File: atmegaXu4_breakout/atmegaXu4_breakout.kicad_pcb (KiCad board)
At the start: 2 copper layers, 20 x 50.5 mm, 36 parts, among them J1 USB_C_Receptacle_USB2.0, J2 Header-West, J3 Header-East, J4 AVR-ISP-6, SW1 nUSR_PB, SW2 nRST_PB, U1 ATmega32U4-MU, U2 AP2127K-3.3, Y1 ABM11-16.000MHZ-12-N1G-T

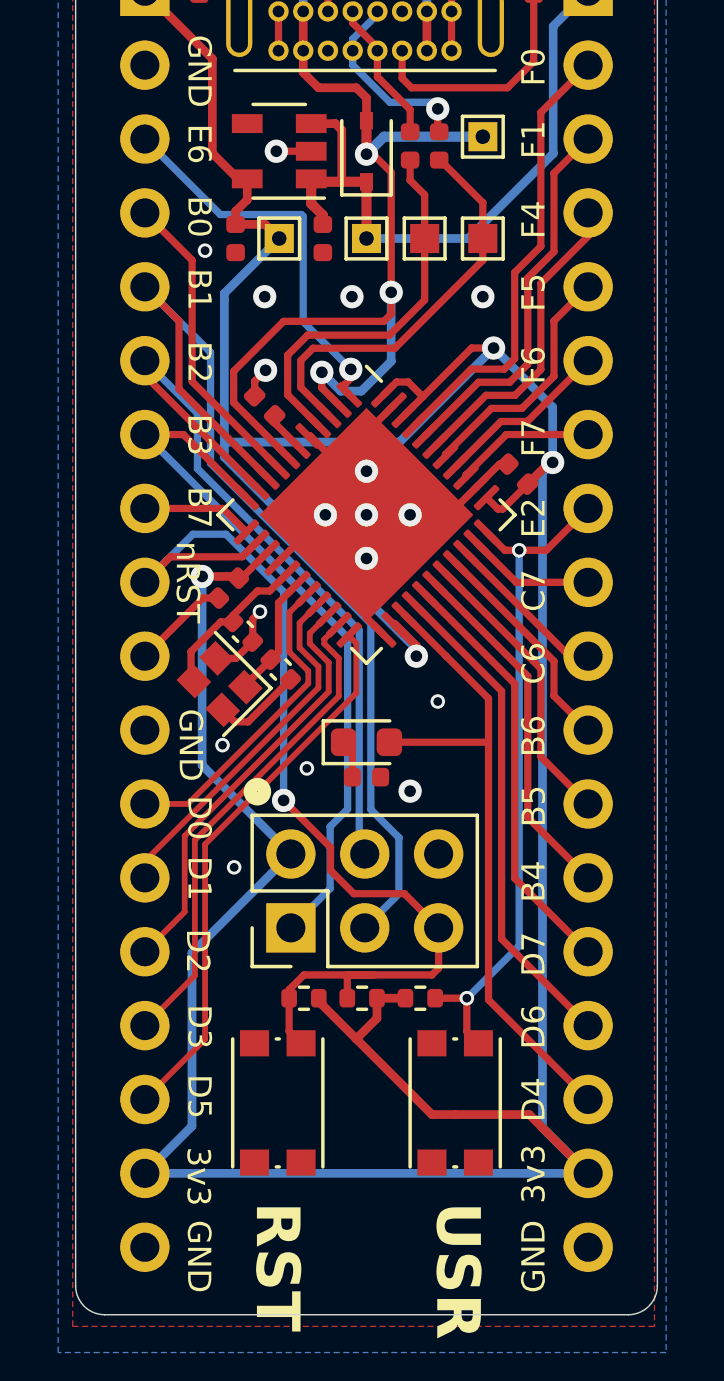
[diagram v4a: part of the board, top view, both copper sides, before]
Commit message: Added CI utils for automating releases
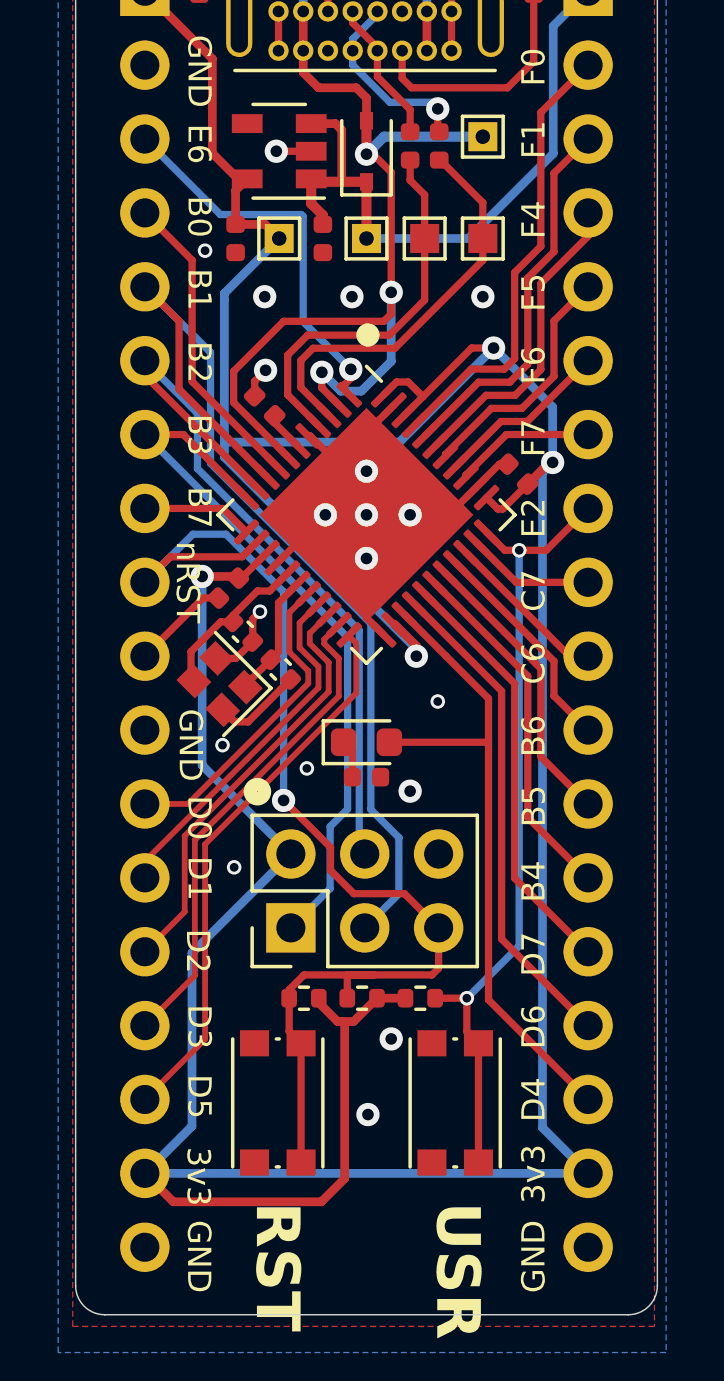
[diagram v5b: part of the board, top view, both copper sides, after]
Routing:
- net PE2: track 23.3 -> 27.4 mm
- net ~{RESET}: track 36.0 -> 40.1 mm
- net +3V3: track 139.2 -> 141.6 mm
- net GND: vias 19 -> 21
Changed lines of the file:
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@@
       (stroke (width 0) (type solid)) (fill solid) (layer "B.SilkS"))
   )
+  (gr_circle (center 146.8 85.6) (end 147 85.6)
+    (stroke (width 0.4) (type default)) (fill none) (layer "F.SilkS"))
   (gr_circle (center 143 101.3) (end 143.2 101.2)
     (stroke (width 0.5) (type solid)) (fill none) (layer "F.SilkS"))
@@
   (via (at 141.8 99.7) (size 0.5) (drill 0.3) (layers "F.Cu" "B.Cu") (free) (net 2))
   (via (at 149.2 98.2) (size 0.5) (drill 0.3) (layers "F.Cu" "B.Cu") (free) (net 2))
+  (via (at 147.6 109.8) (size 0.8) (drill 0.4) (layers "F.Cu" "B.Cu") (net 2))
   (via (at 139.250019 70.281845) (size 0.8) (drill 0.4) (layers "F.Cu" "B.Cu") (net 2))
   (via (at 146.750019 93.281845) (size 0.8) (drill 0.4) (layers "F.Cu" "B.Cu") (net 2))
@@
   (via (at 148.250019 91.781845) (size 0.8) (drill 0.4) (layers "F.Cu" "B.Cu") (net 2))
   (via (at 143.250019 84.281845) (size 0.8) (drill 0.4) (layers "F.Cu" "B.Cu") (net 2))
+  (via (at 146.8 112.4) (size 0.8) (drill 0.4) (layers "F.Cu" "B.Cu") (net 2))
   (via (at 150.750019 84.281845) (size 0.8) (drill 0.4) (layers "F.Cu" "B.Cu") (net 2))
   (segment (start 143.592966 88.624792) (end 143.592966 88.374792) (width 0.25) (layer "F.Cu") (net 3))
@@
   (segment (start 149 107.6) (end 149.230019 107.369981) (width 0.25) (layer "F.Cu") (net 12))
   (segment (start 142.9724 92.7276) (end 142.475 93.225) (width 0.25) (layer "F.Cu") (net 12))
+  (segment (start 144.5 114.05) (end 144.5 109.95) (width 0.25) (layer "F.Cu") (net 12))
   (segment (start 143.9 101.6) (end 145.515018 103.215018) (width 0.25) (layer "F.Cu") (net 12))
   (segment (start 148.055018 104.806844) (end 149.230019 105.981845) (width 0.25) (layer "F.Cu") (net 12))
@@
   (segment (start 146.690019 105.981845) (end 147.86502 104.806844) (width 0.25) (layer "B.Cu") (net 15))
   (segment (start 141.388234 86.20006) (end 139.130019 83.941845) (width 0.25) (layer "B.Cu") (net 15))
-  (segment (start 146.4 109.8) (end 149 112.4) (width 0.3) (layer "F.Cu") (net 16))
+  (segment (start 140.108174 115.4) (end 139.130019 114.421845) (width 0.3) (layer "F.Cu") (net 16))
   (segment (start 142.250019 81.796845) (end 143.265019 81.796845) (width 0.3) (layer "F.Cu") (net 16))
   (segment (start 143.32939 93.081154) (end 142.453491 93.957053) (width 0.25) (layer "F.Cu") (net 16))
   (segment (start 148.049328 88.361216) (end 148.689359 87.721185) (width 0.25) (layer "F.Cu") (net 16))
-  (segment (start 145.11 108.51) (end 146.4 109.8) (width 0.3) (layer "F.Cu") (net 16))
-  (segment (start 149.8 112.4) (end 152.348174 112.4) (width 0.3) (layer "F.Cu") (net 16))
+  (segment (start 145.11 108.555) (end 145.755 109.2) (width 0.3) (layer "F.Cu") (net 16))
+  (segment (start 142.250019 80.631845) (end 142.650019 80.231845) (width 0.3) (layer "F.Cu") (net 16))
   (segment (start 148.464053 96.642505) (end 148.464053 96.288953) (width 0.3) (layer "F.Cu") (net 16))
   (segment (start 151.435913 91.581845) (end 152.292966 90.724792) (width 0.25) (layer "F.Cu") (net 16))
   (segment (start 141.450019 79.350019) (end 142.331845 80.231845) (width 0.3) (layer "F.Cu") (net 16))
+  (segment (start 146 114.6) (end 145.2 115.4) (width 0.3) (layer "F.Cu") (net 16))
   (segment (start 148.09 108.4) (end 147.11 108.4) (width 0.3) (layer "F.Cu") (net 16))
   (segment (start 138.212519 72.864345) (end 139.130019 73.781845) (width 0.35) (layer "F.Cu") (net 16))
@@
   (segment (start 142.453491 93.957053) (end 142.342947 93.957053) (width 0.3) (layer "F.Cu") (net 16))
   (segment (start 153.035913 89.981845) (end 152.292966 90.724792) (width 0.3) (layer "F.Cu") (net 16))
-  (segment (start 142.650019 80.949981) (end 142.650019 80.231845) (width 0.3) (layer "F.Cu") (net 16))
-  (segment (start 147.11 108.4) (end 147.11 109.09) (width 0.3) (layer "F.Cu") (net 16))
   (segment (start 142.331845 80.231845) (end 142.650019 80.231845) (width 0.3) (layer "F.Cu") (net 16))
+  (segment (start 145.755 109.2) (end 145.91 109.2) (width 0.3) (layer "F.Cu") (net 16))
   (segment (start 142.285894 93.9) (end 142.342947 93.957053) (width 0.3) (layer "F.Cu") (net 16))
-  (segment (start 142.250019 81.349981) (end 142.650019 80.949981) (width 0.3) (layer "F.Cu") (net 16))
+  (segment (start 146.31 109.2) (end 145.91 109.2) (width 0.3) (layer "F.Cu") (net 16))
+  (segment (start 145.91 109.2) (end 146 109.29) (width 0.3) (layer "F.Cu") (net 16))
   (segment (start 145.11 108.4) (end 145.11 108.51) (width 0.3) (layer "F.Cu") (net 16))
-  (segment (start 147.11 109.09) (end 146.4 109.8) (width 0.3) (layer "F.Cu") (net 16))
   (segment (start 148.183257 87.215083) (end 148.689359 87.721185) (width 0.25) (layer "F.Cu") (net 16))
   (segment (start 138.212519 71.531845) (end 138.212519 72.864345) (width 0.35) (layer "F.Cu") (net 16))
+  (segment (start 146 109.29) (end 146 114.6) (width 0.3) (layer "F.Cu") (net 16))
   (segment (start 151.119988 86.046795) (end 150.363749 86.046795) (width 0.25) (layer "F.Cu") (net 16))
   (segment (start 150.877755 91.189643) (end 151.269957 91.581845) (width 0.25) (layer "F.Cu") (net 16))
-  (segment (start 142.250019 81.796845) (end 142.250019 81.349981) (width 0.3) (layer "F.Cu") (net 16))
   (segment (start 141.1 93.9) (end 142.285894 93.9) (width 0.3) (layer "F.Cu") (net 16))
-  (segment (start 149 112.4) (end 149.8 112.4) (width 0.3) (layer "F.Cu") (net 16))
-  (segment (start 152.348174 112.4) (end 154.370019 114.421845) (width 0.3) (layer "F.Cu") (net 16))
+  (segment (start 145.2 115.4) (end 140.108174 115.4) (width 0.3) (layer "F.Cu") (net 16))
   (segment (start 153.150019 89.981845) (end 153.035913 89.981845) (width 0.3) (layer "F.Cu") (net 16))
   (segment (start 147.781247 87.215083) (end 148.183257 87.215083) (width 0.25) (layer "F.Cu") (net 16))
+  (segment (start 142.250019 81.796845) (end 142.250019 80.631845) (width 0.3) (layer "F.Cu") (net 16))
+  (segment (start 145.11 108.4) (end 145.11 108.555) (width 0.3) (layer "F.Cu") (net 16))
   (segment (start 141.450019 76.101845) (end 141.450019 79.350019) (width 0.3) (layer "F.Cu") (net 16))
   (segment (start 139.130019 73.781845) (end 141.450019 76.101845) (width 0.3) (layer "F.Cu") (net 16))
+  (segment (start 147.11 108.4) (end 146.31 109.2) (width 0.3) (layer "F.Cu") (net 16))
   (segment (start 148.464053 96.288953) (end 147.71345 95.53835) (width 0.3) (layer "F.Cu") (net 16))
   (segment (start 150.363749 86.046795) (end 148.689359 87.721185) (width 0.25) (layer "F.Cu") (net 16))
@@
   (segment (start 152.931864 93) (end 154.370019 91.561845) (width 0.25) (layer "F.Cu") (net 32))
   (segment (start 150.2 109.55) (end 150.6 109.95) (width 0.25) (layer "F.Cu") (net 32))
+  (segment (start 150.6 114.05) (end 150.6 109.95) (width 0.25) (layer "F.Cu") (net 32))
   (segment (start 150.2 108.4) (end 149.11 108.4) (width 0.25) (layer "F.Cu") (net 32))
   (segment (start 151.503708 93) (end 152 93) (width 0.25) (layer "F.Cu") (net 32))

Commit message: Clean DRC.
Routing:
- net ~{RESET}: track 40.1 -> 43.7 mm, vias 1 -> 0
- net GND: track 38.4 -> 41.2 mm, vias 21 -> 23
- net +3V3: track 141.6 -> 143.0 mm

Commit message: Updated silk logo to everydaydev
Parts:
- moved G*** 3.80 mm to (146.0, 92.0)
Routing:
- net ~{RESET}: track 43.7 -> 45.6 mm
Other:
- board text added: "atmega32u4_breakout"
- board text added: "os.everydaydev.io"
- board text added: "rev B"
- board text removed: "atmega32u4_breakout rev B"

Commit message: Update logo in silkscreen to full everydaydev logo
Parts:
- removed the G*** at (146.0, 92.0)
- added G***: LOGO, atmega32u4_breakout:everydaydev, B.Cu at (148.6, 89.4)
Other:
- board text added: "atmegaXu4_breakout rev-b"
- board text removed: "atmega32u4_breakout"
- board text removed: "rev B"
